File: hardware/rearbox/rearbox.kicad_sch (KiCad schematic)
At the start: 23 parts, among them J1 STDC14, J2 ST-LINK, SW1 Reset, U1 LM4040C33FTA, U2 STM32G473RCTx, Y1 48MHz

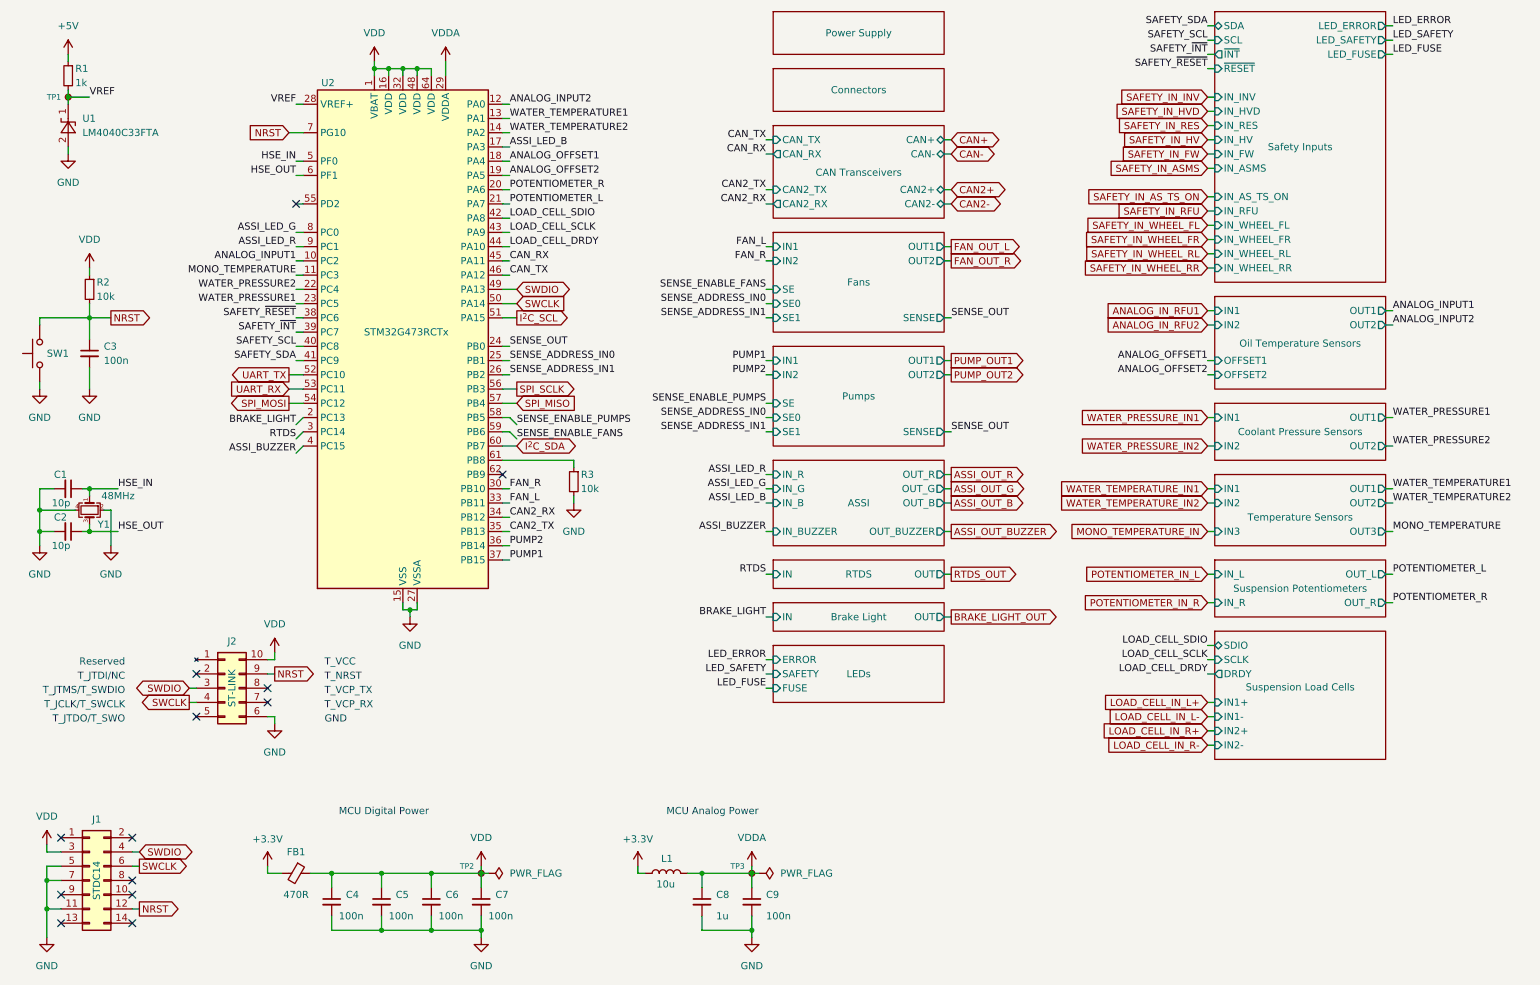
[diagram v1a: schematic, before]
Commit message: Deleted measurement systems for new iteration
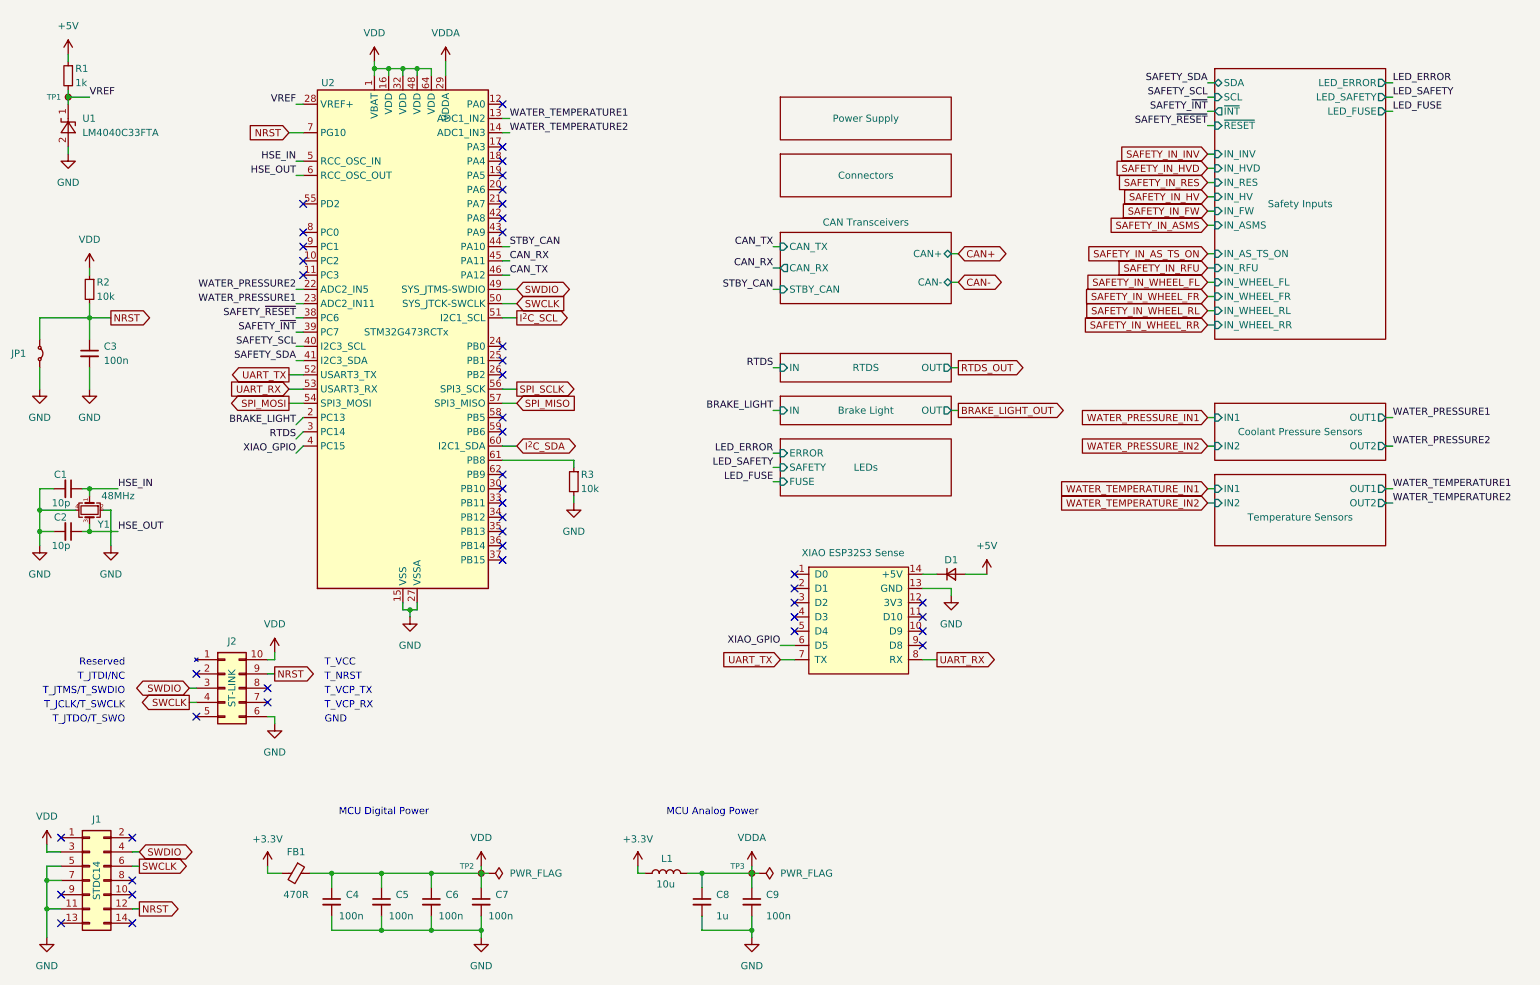
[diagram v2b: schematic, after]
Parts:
- removed SW1: Reset, Button_Switch_SMD:SW_SPST_B3U-1000P, symbol Switch:SW_Push
- added D1: NSVRB751V40T1G, Diode_SMD:D_SOD-323_HandSoldering, symbol Device:D_Small
- added J5: XIAO ESP32S3 Sense, Samacsys:XIAO-ESP32S3-DIP, symbol Connector:Conn_01x04_Socket
- added JP1: Jumper_2_Small_Bridged, Jumper:SolderJumper-2_P1.3mm_Open_TrianglePad1.0x1.5mm, symbol Jumper:Jumper_2_Small_Bridged
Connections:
- net +5V: now also D1.2 (A)
- net GND: now also J5.13 (GND), JP1.2 (B)
- net NRST: now also JP1.1 (A)
- net UART_RX: now also J5.8 (RX)
- net UART_TX: now also J5.7 (TX)
- net ANALOG_INPUT1: no longer names the net of U2.10 (PC2)
- net ANALOG_INPUT2: no longer names the net of U2.12 (PA0)
- net ANALOG_OFFSET1: no longer names the net of U2.18 (PA4)
- net ANALOG_OFFSET2: no longer names the net of U2.19 (PA5)
- net ASSI_BUZZER renamed XIAO_GPIO
- net XIAO_GPIO: now also J5.6 (D5)
- net ASSI_LED_B: no longer names the net of U2.17 (PA3)
- net ASSI_LED_G: no longer names the net of U2.8 (PC0)
- net ASSI_LED_R: no longer names the net of U2.9 (PC1)
- net CAN2_RX: no longer names the net of U2.34 (PB12)
- net CAN2_TX: no longer names the net of U2.35 (PB13)
- net FAN_L: no longer names the net of U2.33 (PB11)
- net FAN_R: no longer names the net of U2.30 (PB10)
- net LOAD_CELL_DRDY renamed STBY_CAN
- net LOAD_CELL_SCLK: no longer names the net of U2.43 (PA9)
- net LOAD_CELL_SDIO: no longer names the net of U2.42 (PA8)
- net MONO_TEMPERATURE: no longer names the net of U2.11 (PC3)
- net POTENTIOMETER_L: no longer names the net of U2.21 (PA7)
- net POTENTIOMETER_R: no longer names the net of U2.20 (PA6)
- net PUMP1: no longer names the net of U2.37 (PB15)
- net PUMP2: no longer names the net of U2.36 (PB14)
- net SENSE_ADDRESS_IN0: no longer names the net of U2.25 (PB1)
- net SENSE_ADDRESS_IN1: no longer names the net of U2.26 (PB2)
- net SENSE_ENABLE_FANS: no longer names the net of U2.59 (PB6)
- net SENSE_ENABLE_PUMPS: no longer names the net of U2.58 (PB5)
- net SENSE_OUT: no longer names the net of U2.24 (PB0)
- new net: D1.1 (K), J5.14 (+5V)
- no-connect marks 13 -> 45
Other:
- removed sheet ASSI
- removed sheet Fans
- removed sheet Oil Temperature Sensors
- removed sheet Pumps
- removed sheet Suspension Load Cells
- removed sheet Suspension Potentiometers
- sheet CAN Transceivers ports: added STBY_CAN; removed CAN2+, CAN2-, CAN2_RX, CAN2_TX
- sheet Temperature Sensors ports: added none; removed IN3, OUT3

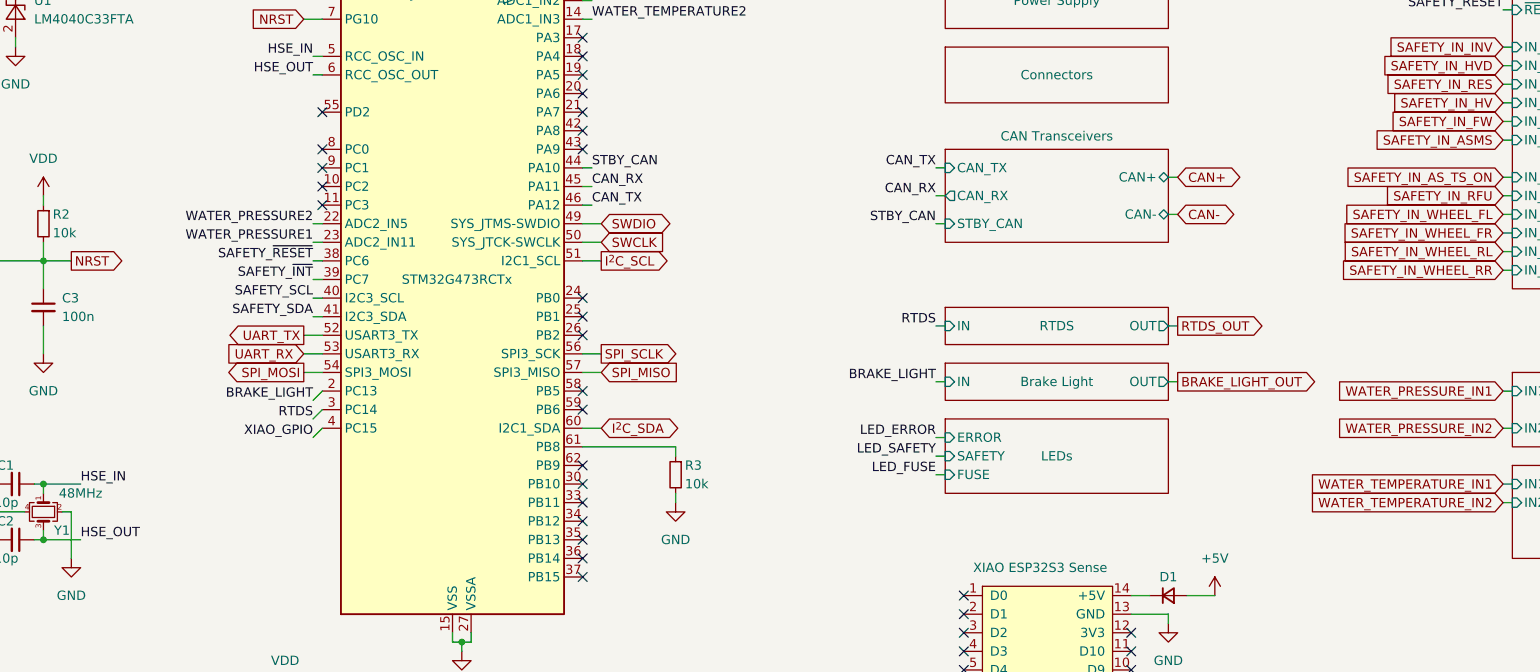
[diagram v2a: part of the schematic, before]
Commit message: Added an auxillary transistor for rear brakelights in case they burn up again and fixed some GNDISO_CAN problems
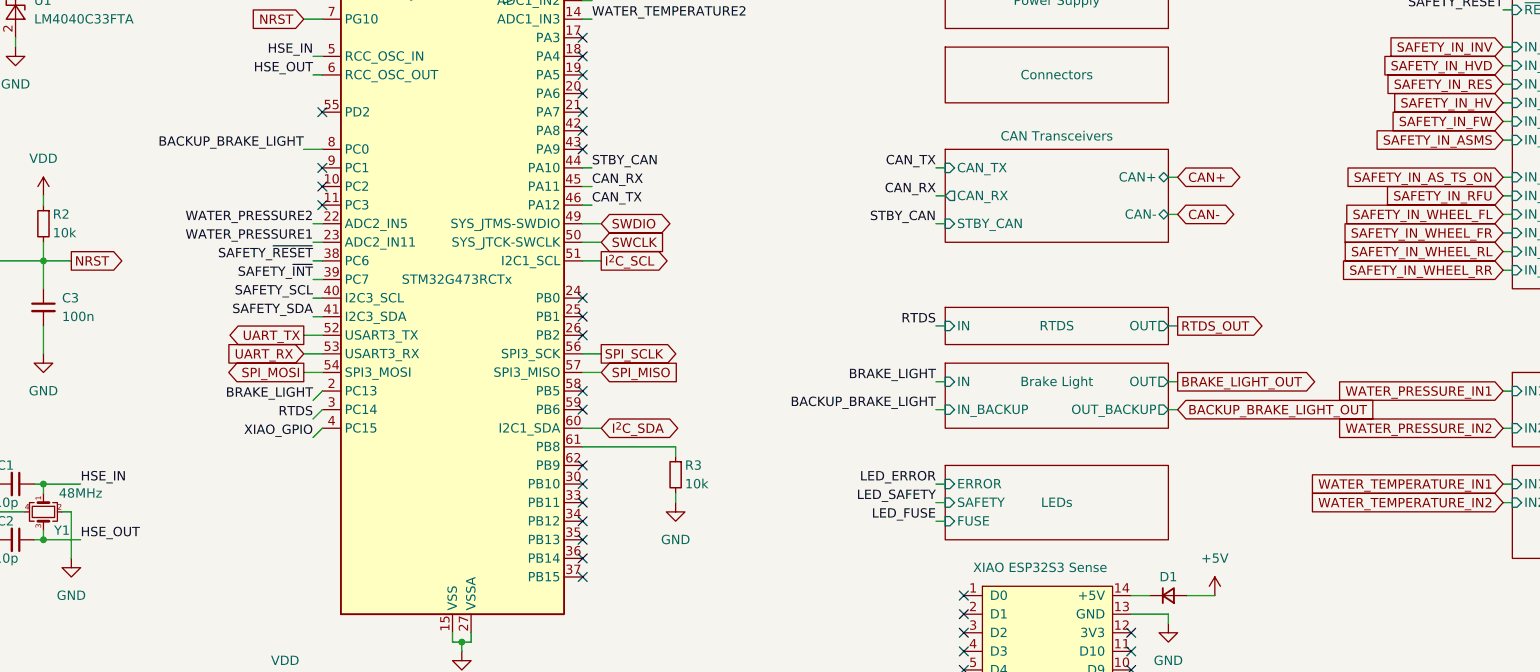
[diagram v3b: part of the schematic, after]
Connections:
- net BACKUP_BRAKE_LIGHT: now reaches U2.8 (PC0)
- no-connect marks 45 -> 44
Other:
- sheet Brake Light ports: added IN_BACKUP, OUT_BACKUP; removed none
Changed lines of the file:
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@@
 	)
 	(no_connect
-		(at 66.04 59.69)
-	)
-	(no_connect
 		(at 101.6 46.99)
 	)
@@
 	(wire
 		(pts
-			(xy 149.86 104.14) (xy 151.13 104.14)
+			(xy 149.86 110.49) (xy 151.13 110.49)
 		)
 		(stroke
@@
 	(wire
 		(pts
+			(xy 63.5 59.69) (xy 66.04 59.69)
+		)
+		(stroke
+			(width 0)
+			(type default)
+		)
+	)
+	(wire
+		(pts
 			(xy 227.33 68.58) (xy 228.6 68.58)
 		)
@@
 	(wire
 		(pts
-			(xy 149.86 101.6) (xy 151.13 101.6)
+			(xy 149.86 107.95) (xy 151.13 107.95)
 		)
 		(stroke
@@
 	(wire
 		(pts
+			(xy 181.61 95.25) (xy 182.88 95.25)
+		)
+		(stroke
+			(width 0)
+			(type default)
+		)
+	)
+	(wire
+		(pts
 			(xy 97.79 173.99) (xy 88.9 173.99)
 		)
@@
 	(wire
 		(pts
+			(xy 149.86 95.25) (xy 151.13 95.25)
+		)
+		(stroke
+			(width 0)
+			(type default)
+		)
+	)
+	(wire
+		(pts
 			(xy 80.01 181.61) (xy 80.01 184.15)
 		)
@@
 	(wire
 		(pts
-			(xy 149.86 99.06) (xy 151.13 99.06)
+			(xy 149.86 105.41) (xy 151.13 105.41)
 		)
 		(stroke
@@
 		)
 	)
+	(label "BACKUP_BRAKE_LIGHT"
+		(at 149.86 95.25 180)
+		(effects
+			(font
+				(size 1.27 1.27)
+			)
+			(justify right bottom)
+		)
+	)
 	(label "WATER_TEMPERATURE2"
 		(at 102.87 41.91 0)
@@
 	)
 	(label "LED_FUSE"
-		(at 149.86 104.14 180)
+		(at 149.86 110.49 180)
 		(effects
 			(font
@@
 		)
 	)
+	(label "BACKUP_BRAKE_LIGHT"
+		(at 63.5 59.69 180)
+		(effects
+			(font
+				(size 1.27 1.27)
+			)
+			(justify right bottom)
+		)
+	)
 	(label "CAN_TX"
 		(at 102.87 67.31 0)
@@
 	)
 	(label "LED_ERROR"
-		(at 149.86 99.06 180)
+		(at 149.86 105.41 180)
 		(effects
 			(font
@@
 	)
 	(label "LED_SAFETY"
-		(at 149.86 101.6 180)
+		(at 149.86 107.95 180)
 		(effects
 			(font
@@
 		)
 	)
+	(global_label "BACKUP_BRAKE_LIGHT_OUT"
+		(shape input)
+		(at 182.88 95.25 0)
+		(fields_autoplaced yes)
+		(effects
+			(font
+				(size 1.27 1.27)
+			)
+			(justify left)
+		)
+		(property "Intersheetrefs" "${INTERSHEET_REFS}"
+			(at 211.1443 95.25 0)
+			(effects
+				(font
+					(size 1.27 1.27)
+				)
+				(justify left)
+				(hide yes)
+			)
+		)
+	)
 	(global_label "SWDIO"
 		(shape bidirectional)
@@
 	)
 	(sheet
-		(at 151.13 96.52)
+		(at 151.13 102.87)
 		(size 30.48 10.16)
 		(exclude_from_sim no)
@@
 		)
 		(property "Sheetname" "LEDs"
-			(at 166.37 101.6 0)
+			(at 166.37 107.95 0)
 			(effects
 				(font
@@
 		)
 		(property "Sheetfile" "leds.kicad_sch"
-			(at 151.13 116.1546 0)
+			(at 151.13 122.5046 0)
 			(effects
 				(font
@@
 		)
 		(pin "FUSE" input
-			(at 151.13 104.14 180)
+			(at 151.13 110.49 180)
 			(effects
 				(font
@@
 		)
 		(pin "ERROR" input
-			(at 151.13 99.06 180)
+			(at 151.13 105.41 180)
 			(effects
 				(font
@@
 		)
 		(pin "SAFETY" input
-			(at 151.13 101.6 180)
+			(at 151.13 107.95 180)
 			(effects
 				(font
@@
 	(sheet
 		(at 151.13 88.9)
-		(size 30.48 5.08)
+		(size 30.48 8.89)
 		(exclude_from_sim no)
 		(in_bom yes)
@@
 			(effects
 				(font
+					(size 1.27 1.27)
+				)
+				(justify right)
+			)
+		)
+		(pin "IN_BACKUP" input
+			(at 151.13 95.25 180)
+			(effects
+				(font
+					(size 1.27 1.27)
+				)
+				(justify left)
+			)
+		)
+		(pin "OUT_BACKUP" output
+			(at 181.61 95.25 0)
+			(effects
+				(font

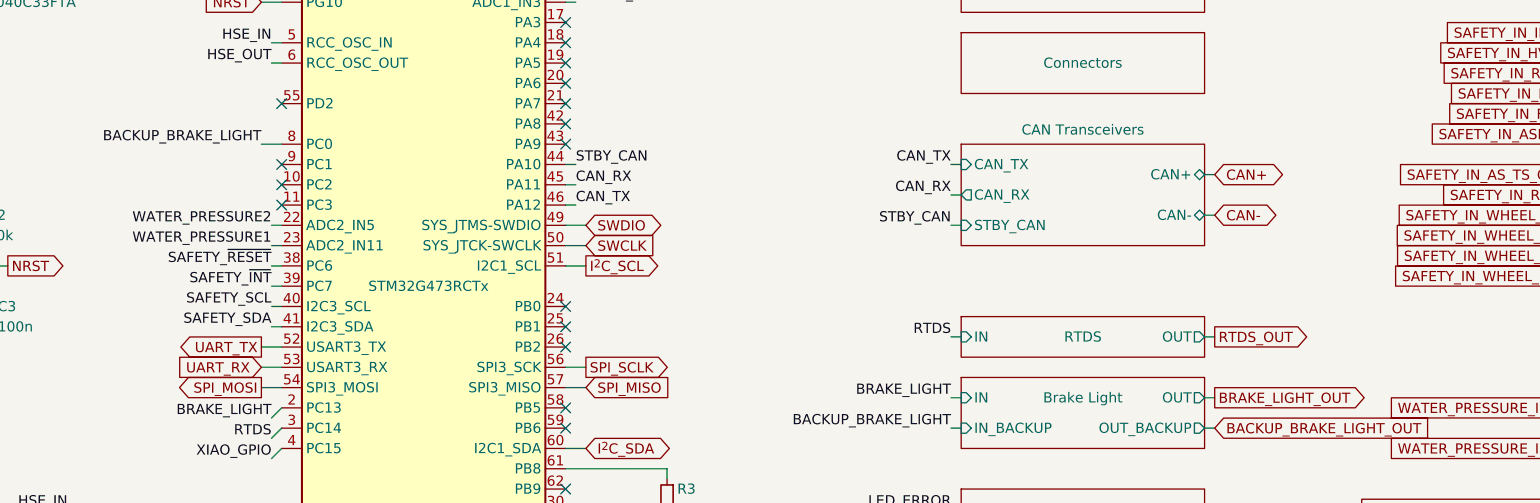
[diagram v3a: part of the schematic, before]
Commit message: Added an auxillary RTDS transistor as a backup
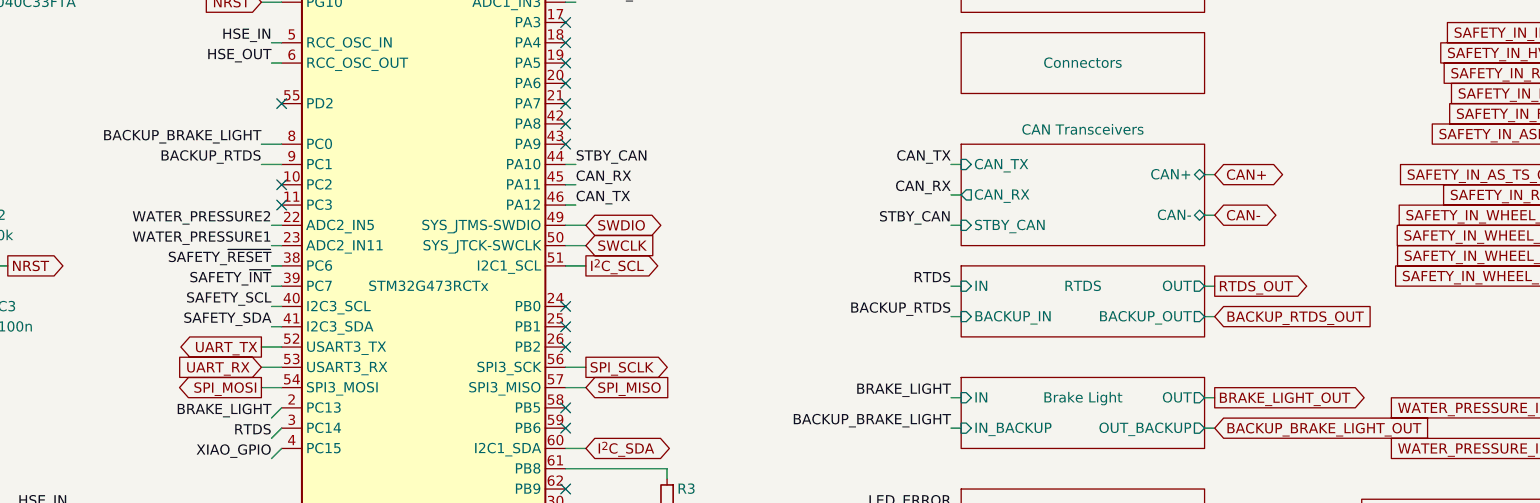
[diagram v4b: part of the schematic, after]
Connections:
- net BACKUP_RTDS: now reaches U2.9 (PC1)
- no-connect marks 44 -> 43
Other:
- sheet RTDS ports: added BACKUP_IN, BACKUP_OUT; removed none
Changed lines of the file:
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@@
 	)
 	(no_connect
-		(at 66.04 62.23)
-	)
-	(no_connect
 		(at 101.6 46.99)
 	)
@@
 	)
 	(no_connect
+		(at 101.6 59.69)
+	)
+	(no_connect
 		(at 101.6 80.01)
 	)
@@
 	)
 	(no_connect
-		(at 101.6 59.69)
-	)
-	(no_connect
 		(at 101.6 105.41)
 	)
@@
 	(wire
 		(pts
+			(xy 149.86 81.28) (xy 151.13 81.28)
+		)
+		(stroke
+			(width 0)
+			(type default)
+		)
+	)
+	(wire
+		(pts
 			(xy 227.33 55.88) (xy 228.6 55.88)
 		)
@@
 	(wire
 		(pts
-			(xy 181.61 83.82) (xy 182.88 83.82)
+			(xy 181.61 77.47) (xy 182.88 77.47)
 		)
 		(stroke
@@
 	(wire
 		(pts
+			(xy 181.61 81.28) (xy 182.88 81.28)
+		)
+		(stroke
+			(width 0)
+			(type default)
+		)
+	)
+	(wire
+		(pts
 			(xy 125.73 173.99) (xy 125.73 172.72)
 		)
@@
 	(wire
 		(pts
+			(xy 63.5 62.23) (xy 66.04 62.23)
+		)
+		(stroke
+			(width 0)
+			(type default)
+		)
+	)
+	(wire
+		(pts
 			(xy 83.82 127) (xy 85.09 127)
 		)
@@
 	(wire
 		(pts
-			(xy 149.86 83.82) (xy 151.13 83.82)
+			(xy 149.86 77.47) (xy 151.13 77.47)
 		)
 		(stroke
@@
 		)
 	)
+	(label "BACKUP_RTDS"
+		(at 149.86 81.28 180)
+		(effects
+			(font
+				(size 1.27 1.27)
+			)
+			(justify right bottom)
+		)
+	)
 	(label "LED_SAFETY"
 		(at 260.35 35.56 0)
@@
 		)
 	)
+	(label "BACKUP_RTDS"
+		(at 63.5 62.23 180)
+		(effects
+			(font
+				(size 1.27 1.27)
+			)
+			(justify right bottom)
+		)
+	)
 	(label "XIAO_GPIO"
 		(at 151.13 133.35 180)
@@
 	)
 	(label "RTDS"
-		(at 149.86 83.82 180)
+		(at 149.86 77.47 180)
 		(effects
 			(font
@@
 		)
 	)
+	(global_label "BACKUP_RTDS_OUT"
+		(shape input)
+		(at 182.88 81.28 0)
+		(fields_autoplaced yes)
+		(effects
+			(font
+				(size 1.27 1.27)
+			)
+			(justify left)
+		)
+		(property "Intersheetrefs" "${INTERSHEET_REFS}"
+			(at 203.6452 81.28 0)
+			(effects
+				(font
+					(size 1.27 1.27)
+				)
+				(justify left)
+				(hide yes)
+			)
+		)
+	)
 	(global_label "WATER_PRESSURE_IN2"
 		(shape input)
@@
 	(global_label "RTDS_OUT"
 		(shape output)
-		(at 182.88 83.82 0)
+		(at 182.88 77.47 0)
 		(fields_autoplaced yes)
 		(effects
@@
 		)
 		(property "Intersheetrefs" "${INTERSHEET_REFS}"
-			(at 195.1785 83.82 0)
+			(at 195.1785 77.47 0)
 			(effects
 				(font
@@
 	)
 	(sheet
-		(at 151.13 81.28)
-		(size 30.48 5.08)
+		(at 151.13 74.93)
+		(size 30.48 8.89)
 		(exclude_from_sim no)
 		(in_bom yes)
@@
 		)
 		(property "Sheetname" "RTDS"
-			(at 166.37 83.82 0)
+			(at 166.37 77.47 0)
 			(effects
 				(font
@@
 		)
 		(property "Sheetfile" "ready_to_drive_sound.kicad_sch"
-			(at 151.13 100.9146 0)
+			(at 151.13 94.5646 0)
 			(effects
 				(font
@@
 		)
 		(pin "OUT" output
-			(at 181.61 83.82 0)
+			(at 181.61 77.47 0)
 			(effects
 				(font
@@
 		)
 		(pin "IN" input
-			(at 151.13 83.82 180)
+			(at 151.13 77.47 180)
 			(effects
 				(font
@@
 			)
 		)
+		(pin "BACKUP_IN" input
+			(at 151.13 81.28 180)
+			(effects
+				(font
+					(size 1.27 1.27)
+				)
+				(justify left)
+			)
+		)
+		(pin "BACKUP_OUT" output
+			(at 181.61 81.28 0)
+			(effects
+				(font
+					(size 1.27 1.27)
+				)
+				(justify right)
+			)
+		)
